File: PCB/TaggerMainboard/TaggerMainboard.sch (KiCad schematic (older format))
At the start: 64 parts

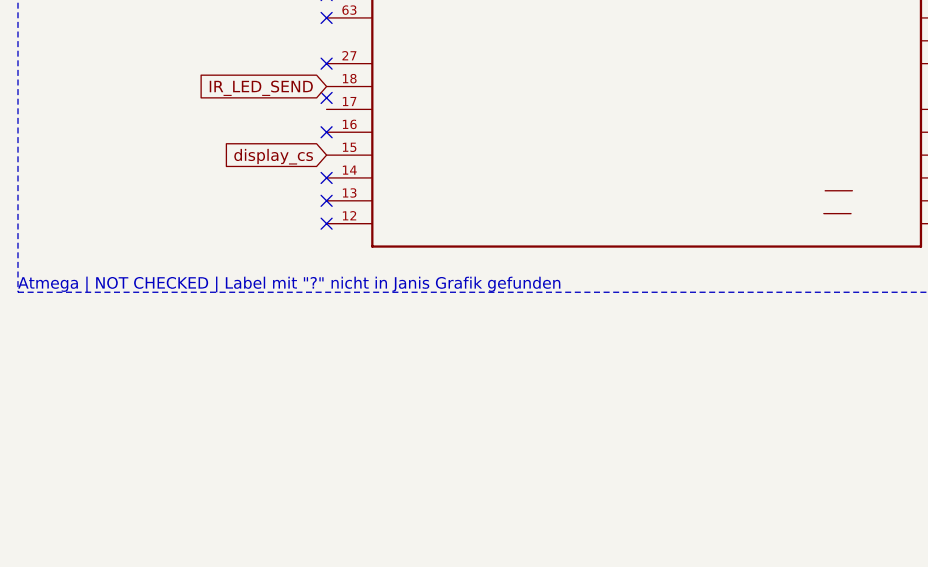
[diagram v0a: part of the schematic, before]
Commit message: Notiz am Atmega angepasst
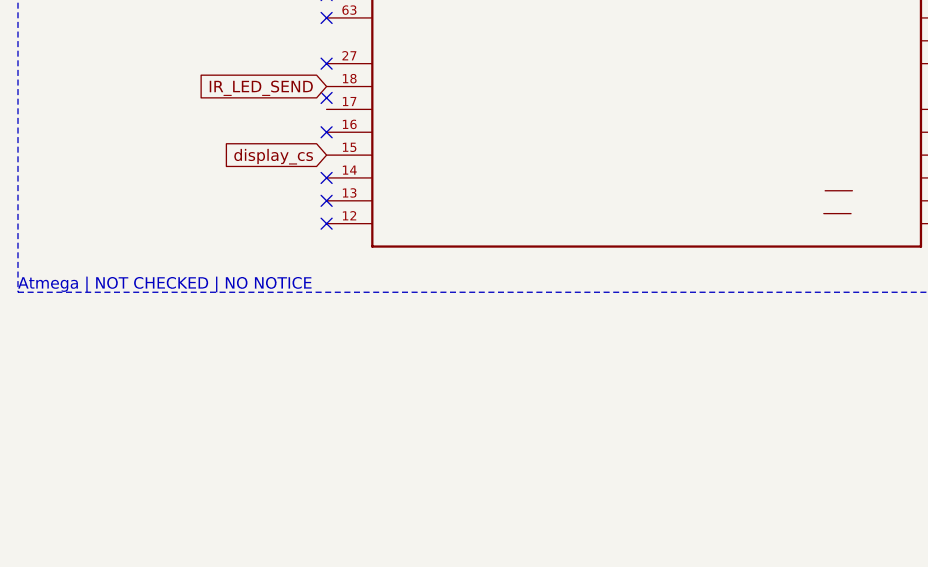
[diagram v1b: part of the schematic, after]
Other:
- note added: "Atmega | NOT CHECKED | NO NOTICE"
- note removed: "Atmega | NOT CHECKED | Label mit "?" nicht in Janis Grafik gefunden"
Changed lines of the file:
@@
 	650  650  5550 650
 Text Notes 650  7250 0    50   ~ 0
-Atmega | NOT CHECKED | Label mit "?" nicht in Janis Grafik gefunden
+Atmega | NOT CHECKED | NO NOTICE
 Wire Wire Line
 	2000 2750 1900 2750

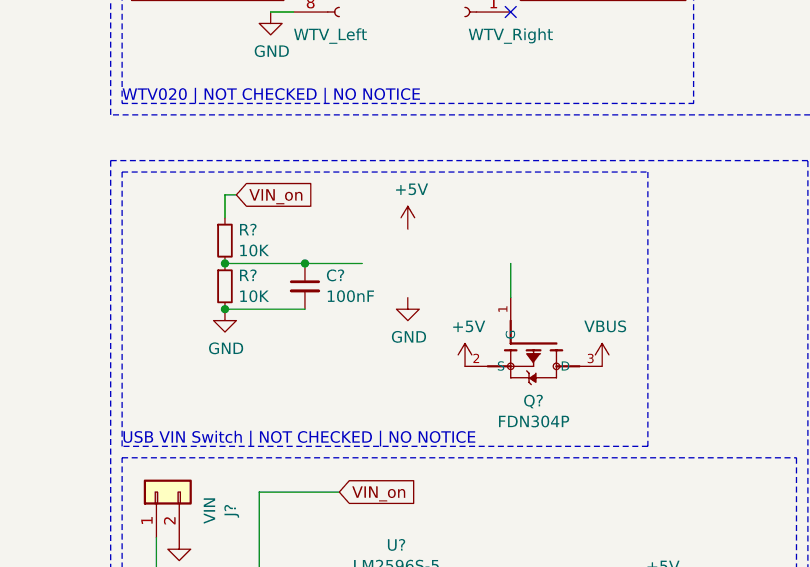
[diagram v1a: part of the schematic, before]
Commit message: LMV hinzugefügt
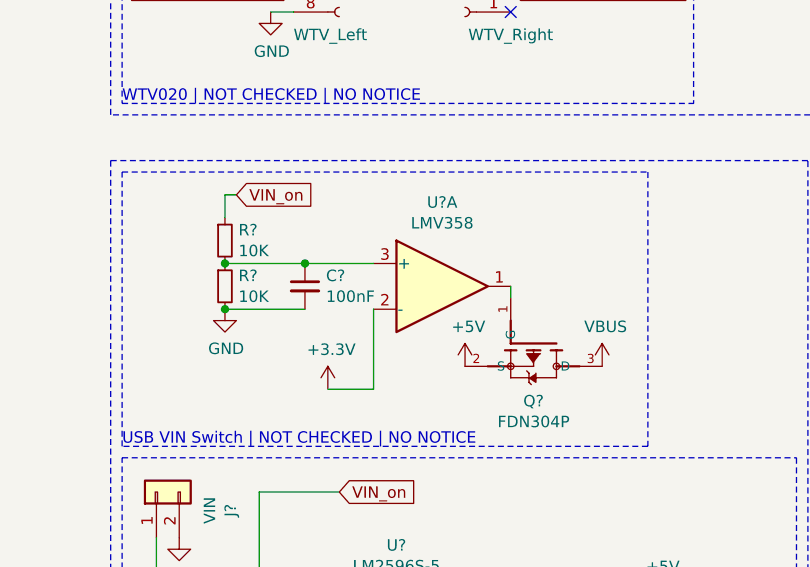
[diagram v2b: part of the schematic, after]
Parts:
- added U?: LMV358, symbol Amplifier_Operational:LMV358
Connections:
- wire segments 101 -> 103
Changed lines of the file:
@@
 	0    1    1    0
 $EndComp
-Wire Wire Line
-	10100 7100 10100 7250
 $Comp
 L power:+5V #PWR?
@@
 F 3 "" H 10500 7550 50  0001 C CNN
 	1    10500 7550
-	1    0    0    -1
-$EndComp
-$Comp
-L power:+5V #PWR?
-U 1 1 5C96BA6B
-P 9650 6950
-F 0 "#PWR?" H 9650 6800 50  0001 C CNN
-F 1 "+5V" H 9665 7123 50  0000 C CNN
-F 2 "" H 9650 6950 50  0001 C CNN
-F 3 "" H 9650 6950 50  0001 C CNN
-	1    9650 6950
-	1    0    0    -1
-$EndComp
-$Comp
-L power:GND #PWR?
-U 1 1 5C96BBB1
-P 9650 7250
-F 0 "#PWR?" H 9650 7000 50  0001 C CNN
-F 1 "GND" H 9655 7077 50  0000 C CNN
-F 2 "" H 9650 7250 50  0001 C CNN
-F 3 "" H 9650 7250 50  0001 C CNN
-	1    9650 7250
 	1    0    0    -1
 $EndComp
@@
 $EndComp
 Connection ~ 8850 7300
-Wire Wire Line
-	9200 7100 9450 7100
 Connection ~ 9200 7100
 Wire Wire Line
@@
 Wire Wire Line
 	14300 4250 14900 4250
+$Comp
+L Amplifier_Operational:LMV358 U?
+U 1 1 5C9D3923
+P 9800 7200
+F 0 "U?" H 9800 7567 50  0000 C CNN
+F 1 "LMV358" H 9800 7476 50  0000 C CNN
+F 2 "" H 9800 7200 50  0001 C CNN
+F 3 "http://www.ti.com/lit/ds/symlink/lmv324.pdf" H 9800 7200 50  0001 C CNN
+	1    9800 7200
+	1    0    0    -1
+$EndComp
+Wire Wire Line
+	10100 7200 10100 7250
+Wire Wire Line
+	9200 7100 9500 7100
+Wire Wire Line
+	9500 7300 9500 7650
+Wire Wire Line
+	9500 7650 9300 7650
+$Comp
+L power:+3.3V #PWR?
+U 1 1 5C9DC200
+P 9300 7650
+F 0 "#PWR?" H 9300 7500 50  0001 C CNN
+F 1 "+3.3V" H 9315 7823 50  0000 C CNN
+F 2 "" H 9300 7650 50  0001 C CNN
+F 3 "" H 9300 7650 50  0001 C CNN
+	1    9300 7650
+	1    0    0    -1
+$EndComp
 $EndSCHEMATC

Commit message: Footsprints zugewiesen
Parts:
- C5, C7: renamed from C?; footprint (none) -> Capacitor_SMD:CP_Elec_6.3x5.8
- C6: renamed from C?; footprint (none) -> Capacitor_SMD:C_0805_2012Metric
- D4: renamed from D?; footprint (none) -> Diode_SMD:D_0805_2012Metric
- J16: renamed from J?; footprint (none) -> Connector_JST:JST_PH_B8B-PH-K_1x08_P2.00mm_Vertical
- J2, J5: renamed from J?; footprint (none) -> Connector_PinHeader_2.54mm:PinHeader_1x08_P2.54mm_Vertical
- J3: renamed from J?; footprint (none) -> Connector_PinSocket_2.54mm:PinSocket_1x05_P2.54mm_Vertical
- L1: renamed from L?; footprint (none) -> Inductor_SMD:L_0805_2012Metric
- R6, R7: renamed from R?; footprint (none) -> Resistor_SMD:R_0805_2012Metric
- gave numbers to parts that had none: 54

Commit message: Footprints angepasst
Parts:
- removed D1: LED_RX_red, LED_SMD:LED_1206_3216Metric, symbol Device:D_Small
- removed D2: LED_TX_red, LED_SMD:LED_1206_3216Metric, symbol Device:D_Small
- removed Q2: FDN304P, SOT95P240X120-3N, symbol FDN340P:FDN340P
- added D1: LED_RX_red, Diode_SMD:D_1206_3216Metric, symbol Device:LED_Small
- added D2: LED_TX_red, Diode_SMD:D_1206_3216Metric, symbol Device:LED_Small
- added Q2: FDN304P, FDN304P:SSOT-3, symbol FDN304P:FDN304P
- J3: footprint Connector_PinSocket_2.54mm:PinSocket_1x05_P2.54mm_Vertical -> Infinitag:Infinitag_ESP_Shield
- U1: footprint TQFP100-0.5-14X14MM -> MCU-ATMEGA2560-16AU_TQFP100_:TQFP100-0.5-14X14MM
- U3: footprint (none) -> LMV358AM8X:SOIC127P620X172-8N
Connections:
- net Sensor_GND is gone; now on net GND: J15.2 (Pin_2), J9.2 (Pin_2)
- net +5V: now also Q2.2 (S)
- net LED_RX: now also D1.1 (K)
- net LED_TX: now also D2.1 (K)
- net VBUS: now also Q2.3 (D)
- net at R4.1: now also D1.2 (A)
- net at R5.2: now also D2.2 (A)
- net at U3.1: now also Q2.1 (G)

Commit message: Schematic fertiggestellt, Libs hinzugefügt, PCB Design erstellt
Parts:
- removed J17: JST_PH_Display, Connector_JST:JST_PH_B7B-PH-K_1x07_P2.00mm_Vertical, symbol Connector_Generic:Conn_01x07
- removed J2: WTV_Left, Connector_PinHeader_2.54mm:PinHeader_1x08_P2.54mm_Vertical, symbol Connector:Conn_01x08_Female
- removed J5: WTV_Right, Connector_PinHeader_2.54mm:PinHeader_1x08_P2.54mm_Vertical, symbol Connector:Conn_01x08_Female
- removed Q1, Q3: BSS138, Package_TO_SOT_SMD:SOT-23, symbol Transistor_FET:BSS138
- removed R10: 1K, Resistor_SMD:R_0805_2012Metric, symbol Device:R_Small
- removed R12, R13, R14, R15, R16, R17, R9: 10K, Resistor_SMD:R_0805_2012Metric, symbol Device:R_Small
- added C10, C15: 220uF/16V, Capacitor_SMD:CP_Elec_6.3x5.8, symbol Device:CP_Small
- added J12: JST_PH_IrLED, Connector_JST:JST_PH_B4B-PH-K_1x04_P2.00mm_Vertical, symbol Connector_Generic:Conn_01x04
- added J17: Infinitag_Shield, Infinitag:Infinitag_Shield, symbol Connector_Generic:Conn_01x10
- added J3: DFPlayer, Infinitag:DFPlayer, symbol Connector_Generic:Conn_01x16
- added J9: JST_PH_Display, Connector_JST:JST_PH_B5B-PH-K_1x05_P2.00mm_Vertical, symbol Connector_Generic:Conn_01x05
- added RN1, RN2: Array 10K, Resistor_SMD:R_Array_Convex_4x0603, symbol Device:R_Pack04
- added RN3: Array 470, Resistor_SMD:R_Array_Convex_4x0603, symbol Device:R_Pack04
- added U2: IRLML2502, IRLML2502TRPBF:SOT23, symbol IRLML2502TRPBF:IRLML2502TRPBF
- C11: renamed from C10; value C_Small -> 100nF
- D1, D2: footprint Diode_SMD:D_1206_3216Metric -> LED_SMD:LED_1206_3216Metric
- J5: renamed from J6; footprint (none) -> Infinitag:Micro USB Jack
- L1: footprint Inductor_SMD:L_0805_2012Metric -> Inductor_SMD:L_Wuerth_HCI-1350
- R4: value 1K -> 10K
- R5: value 1K -> 50 Ohm
- R8: value 10K -> 1K
- renumbered C11 to C12, C12 to C13, C8 to C7, C7 to C8, J12 to J13, J13 to J14, J14 to J15, J15 to J16, J16 to J18, J4 to J2, J3 to J4, J7 to J6, J8 to J7, J9 to J8, Q2 to Q1, R18 to R10, R19 to R11, R11 to R9, U2 to U3, U3 to U4, U4 to U5, U5 to U6
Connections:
- net +3V3: now also J17.2 (Pin_2); no longer R8.1
- net +5V: now also C12.1, U6.19 (~RESET~), U6.20 (VCC), U6.4 (VCCIO), C10.1, C15.1, J12.1 (Pin_1), J17.1 (Pin_1), J3.1 (Pin_1), RN1.5 (R4.2), RN1.6 (R3.2), RN1.7 (R2.2), RN1.8 (R1.2); no longer R4.2, R5.1
- net GND: now also R4.2, U6.18 (GND), U6.21 (GND), U6.25 (AGND), U6.26 (TEST), U6.7 (GND), C15.2, J12.2 (Pin_2), J17.3 (Pin_3), J3.7 (Pin_7), RN2.5 (R4.2), RN2.6 (R3.2), RN2.7 (R2.2), RN2.8 (R1.2), U2.2 (S)
- net IR_LED_SEND: now also R4.1, U2.1 (G)
- net MOSI: now also J9.2 (Pin_2)
- net SCK: now also J9.1 (Pin_1)
- net display_cs: now also J9.5 (Pin_5)
- net display_dc: now also J9.4 (Pin_4)
- net display_reset: now also J9.3 (Pin_3)
- net key_info: now also RN2.3 (R3.1)
- net key_reload: now also RN2.2 (R2.1)
- net key_special: now also RN2.4 (R4.1)
- net key_trigger: now also RN2.1 (R1.1)
- net ledbar_left: now also RN3.7 (R2.2); no longer U1.59 ((A14)PC6)
- net ledbar_right: now also RN3.8 (R1.2); no longer U1.60 ((A15)PC7)
- net DF_TX: now reaches U1.12 (PH0(RXD2))
- net DF_TX: now also J3.3 (Pin_3)
- net DF_RX: now reaches U1.13 (PH1(TXD2))
- net DF_RX: now also R8.1
- net DF_BUSY: now reaches U1.17 (PH5(OC4C))
- net DF_BUSY: now also J3.16 (Pin_16)
- net Shield_D0: now reaches U1.24 ((OC1A/PCINT5)PB5)
- net Shield_D0: now also J17.6 (Pin_6)
- net Shield_D1: now reaches U1.25 ((OC1B/PCINT6)PB6)
- net Shield_D1: now also J17.7 (Pin_7)
- net Shield_D2: now reaches U1.26 ((OC0A/OC1C/PCINT7)PB7)
- net Shield_D2: now also J17.8 (Pin_8)
- net at U1.33 (XTAL2), Y1.1: now also R1.1
- net at U1.34 (XTAL1), Y1.3: now also R1.2
- net at U1.58 ((A13)PC5): now also RN3.3 (R3.1)
- net Shield_RX: now reaches U1.63 (PJ0(RXD3/PCINT9))
- net Shield_RX: now also J17.4 (Pin_4)
- net Shield_TX: now reaches U1.64 (PJ1(TXD3/PCINT10))
- net Shield_TX: now also J17.5 (Pin_5)
- net Shield_A0: now reaches U1.90 ((ADC7/TDI)PF7)
- net Shield_A0: now also J17.9 (Pin_9)
- net Shield_A1: now reaches U1.91 ((ADC6/TDO)PF6)
- net Shield_A1: now also J17.10 (Pin_10)
- net at D3.2 (A): now also RN1.4 (R4.1)
- net at D2.2 (A): now also RN1.2 (R2.1); no longer R5.2
- net at D1.2 (A): now also RN1.1 (R1.1); no longer R4.1
- net ATV020_CLK_5V: no longer names the net of U1.48 ((XCK1)PD5)
- net ATV020_DATA_5V: no longer names the net of U1.47 ((ICP1)PD4)
- net WTV020_BUSY: no longer names the net of U1.49 ((T1)PD6)
- net WTV020_CLK_3V3: no longer names the net of R8.2
- net WTV020_CLK_3V3: now also J3.2 (Pin_2)
- net WTV020_SPK+ renamed DF_SPK+
- net DF_SPK+: now also J3.6 (Pin_6)
- net WTV020_SPK- renamed DF_SPK-
- net DF_SPK-: now also J3.8 (Pin_8)
- net battery_sense: no longer names the net of U1.78 ((AD0)PA0)
- new net: RN3.2 (R2.1), U1.59 ((A14)PC6)
- new net: RN3.1 (R1.1), U1.60 ((A15)PC7)
- new net: R5.2, U2.3 (D)
- new net IR_LED_GND: C10.2, J12.4 (Pin_4), R5.1
- new net IR_SK_Data: J12.3 (Pin_3), RN3.6 (R3.2)
- no-connect marks 78 -> 74
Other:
- note added: "Checklist\n-----------------------\n[ ] Prüfen ob der DFPlayer korrekt angeschlossen ist\n[ ] USB Footprint ist noch nicht der korrekte\n[ ] ESP Shield prüfen, ob so gut für uns\n[ ] Infinitag Shield prüfen, ob so gut für uns"
- note added: "DFPlayer Anschlüsse | NOT CHECKED | NO NOTICE"
- note added: "DFPlayer | NOT CHECKED | NO NOTICE"
- note added: "IR LED | NOT CHECKED | NO NOTICE"
- note removed: "Bi Level Shift WTV020| NOT CHECKED | NO NOTICE"
- note removed: "WTV Anschlüsse | NOT CHECKED | NO NOTICE"
- note removed: "WTV020 | NOT CHECKED | NO NOTICE"
- moved on the sheet: C5, C6, C8, D1, D2, D3, D4, J1, J11, J14, J16, J18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

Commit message: Keypad + Bohrungen + Logo & Co
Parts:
- D5: footprint Diode_SMD:D_0805_2012Metric -> Diode_SMD:D_1206_3216Metric
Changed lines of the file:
@@
 F 0 "D5" V 11404 2418 50  0000 L CNN
 F 1 "CD1206-S01575" V 11495 2418 50  0000 L CNN
-F 2 "Diode_SMD:D_0805_2012Metric" V 11450 2350 50  0001 C CNN
+F 2 "Diode_SMD:D_1206_3216Metric" V 11450 2350 50  0001 C CNN
 F 3 "~" V 11450 2350 50  0001 C CNN
 	1    11450 2350

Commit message: Anpassungen
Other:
- note added: "Checklist\n-----------------------\n[ ] DF Player: Pin-Abstand falsch\n[ ] Dioden Footprint falsch\n[ ] Resonator Footprint falsch\n[ ] ESP Shield prüfen, ob so gut für uns\n[ ] Infinitag Shield prüfen, ob so gut für uns"
- note removed: "Checklist\n-----------------------\n[ ] Prüfen ob der DFPlayer korrekt angeschlossen ist\n[ ] USB Footprint ist noch nicht der korrekte\n[ ] ESP Shield prüfen, ob so gut für uns\n[ ] Infinitag Shield prüfen, ob so gut für uns"
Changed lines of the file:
@@
 NoConn ~ 4800 1750
 Text Notes 600  11050 0    50   ~ 0
-Checklist\n-----------------------\n[  ] Prüfen ob der DFPlayer korrekt angeschlossen ist\n[  ] USB Footprint ist noch nicht der korrekte\n[  ] ESP Shield prüfen, ob so gut für uns\n[  ] Infinitag Shield prüfen, ob so gut für uns
+Checklist\n-----------------------\n[  ] DF Player: Pin-Abstand falsch\n[  ] Dioden Footprint falsch\n[  ] Resonator Footprint falsch\n[  ] ESP Shield prüfen, ob so gut für uns\n[  ] Infinitag Shield prüfen, ob so gut für uns
 $Comp
 L Connector_Generic:Conn_01x05 J9

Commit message: Anpassungen
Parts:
- D4: footprint Diode_SMD:D_0805_2012Metric -> Diode_SMD:D_SMA
- Y1: footprint Crystal:Resonator_SMD-3Pin_7.2x3.0mm -> Crystal:Resonator_SMD_muRata_CSTxExxV-3Pin_3.0x1.1mm
- renumbered C15 to C13, C13 to C14, J11 to J10, J7 to J11, J8 to J7, J9 to J8, J10 to J9, RN3 to RN1, RN1 to RN2, RN2 to RN3
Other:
- note added: "Checklist\n-----------------------\n[ ] ESP Shield prüfen, ob so gut für uns\n[ ] Infinitag Shield prüfen, ob so gut für uns"
- note removed: "Checklist\n-----------------------\n[ ] DF Player: Pin-Abstand falsch\n[ ] Dioden Footprint falsch\n[ ] Resonator Footprint falsch\n[ ] ESP Shield prüfen, ob so gut für uns\n[ ] Infinitag Shield prüfen, ob so gut für uns"
